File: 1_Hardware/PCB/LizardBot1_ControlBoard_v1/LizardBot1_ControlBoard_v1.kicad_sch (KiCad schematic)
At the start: 6 parts

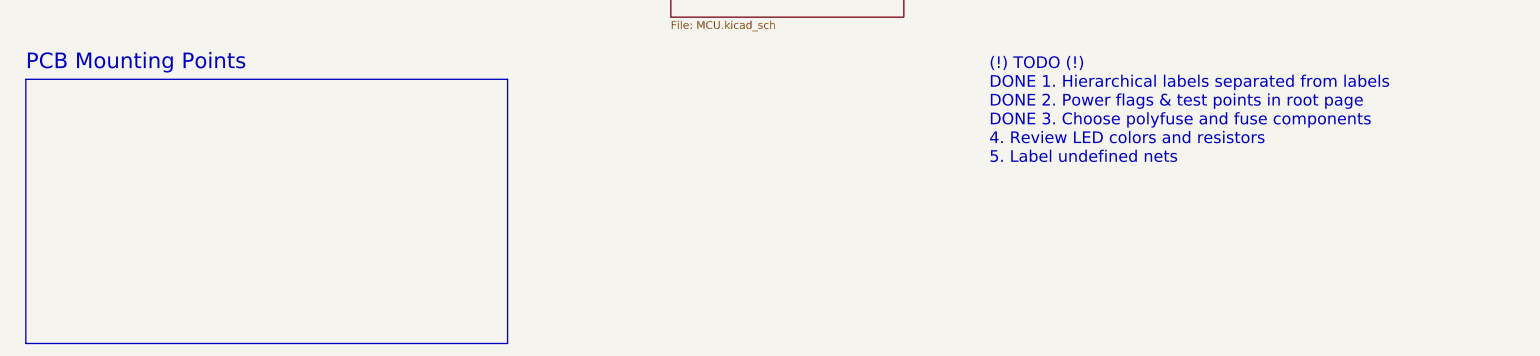
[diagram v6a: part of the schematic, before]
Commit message: Updated schematics. Assigned footprints. Added BOM to /4_Docs.
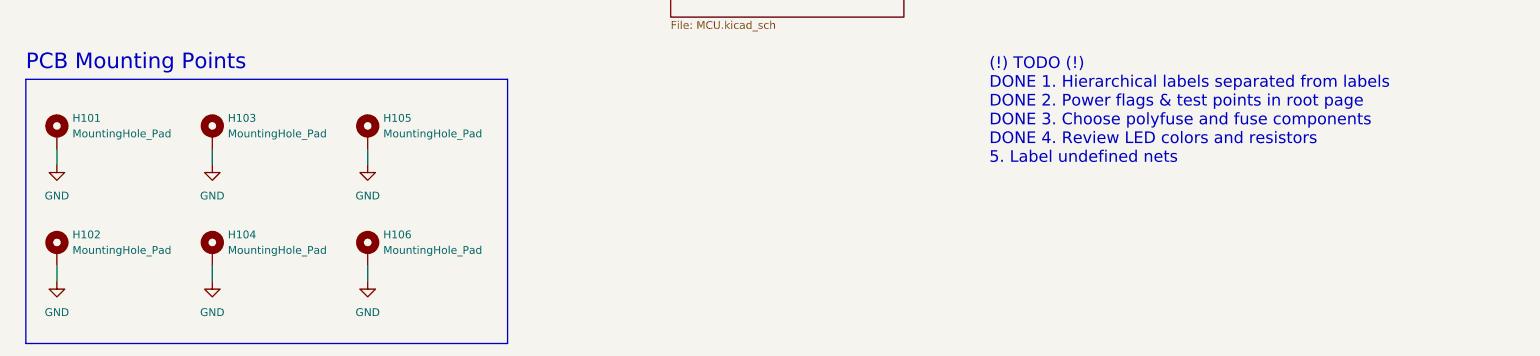
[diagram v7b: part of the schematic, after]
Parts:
- added H101, H102, H103, H104, H105, H106: MountingHole_Pad, MountingHole:MountingHole_3.2mm_M3_Pad_Via, symbol Mechanical:MountingHole_Pad
- TP101, TP102, TP103, TP104, TP105, TP106: footprint (none) -> TestPoint:TestPoint_Pad_D1.5mm
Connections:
- net GND: now also H101.1, H102.1, H103.1, H104.1, H105.1, H106.1
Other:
- note added: "(!) TODO (!) DONE 1. Hierarchical labels separated from labels DONE 2. Power flags & test points in root page DONE 3. Choose polyfuse and fuse components DONE 4. Review LED colors and resistors 5. Label undefined nets"
- note removed: "(!) TODO (!) DONE 1. Hierarchical labels separated from labels DONE 2. Power flags & test points in root page DONE 3. Choose polyfuse and fuse components 4. Review LED colors and resistors 5. Label undefined nets"

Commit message: Added PCB Stack and Design Rules. Added PCB Layout file.
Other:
- note removed: "(!) TODO (!) DONE 1. Hierarchical labels separated from labels DONE 2. Power flags & test points in root page DONE 3. Choose polyfuse and fuse components DONE 4. Review LED colors and resistors 5. Label undefined nets"
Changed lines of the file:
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@@
-		)
-	)
-	(text "(!) TODO (!)\nDONE 1. Hierarchical labels separated from labels\nDONE 2. Power flags & test points in root page\nDONE 3. Choose polyfuse and fuse components\nDONE 4. Review LED colors and resistors\n5. Label undefined nets"
-		(exclude_from_sim no)
-		(at 177.8 161.29 0)
-		(effects
-			(font
-				(size 1.905 1.905)
-			)
-			(justify left bottom)
 		)
 	)
